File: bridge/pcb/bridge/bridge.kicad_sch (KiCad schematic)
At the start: 3 parts, among them J1 Motor_Control_Connector, J2 General_Use_Terminal, J3 Tachometer_Terminal

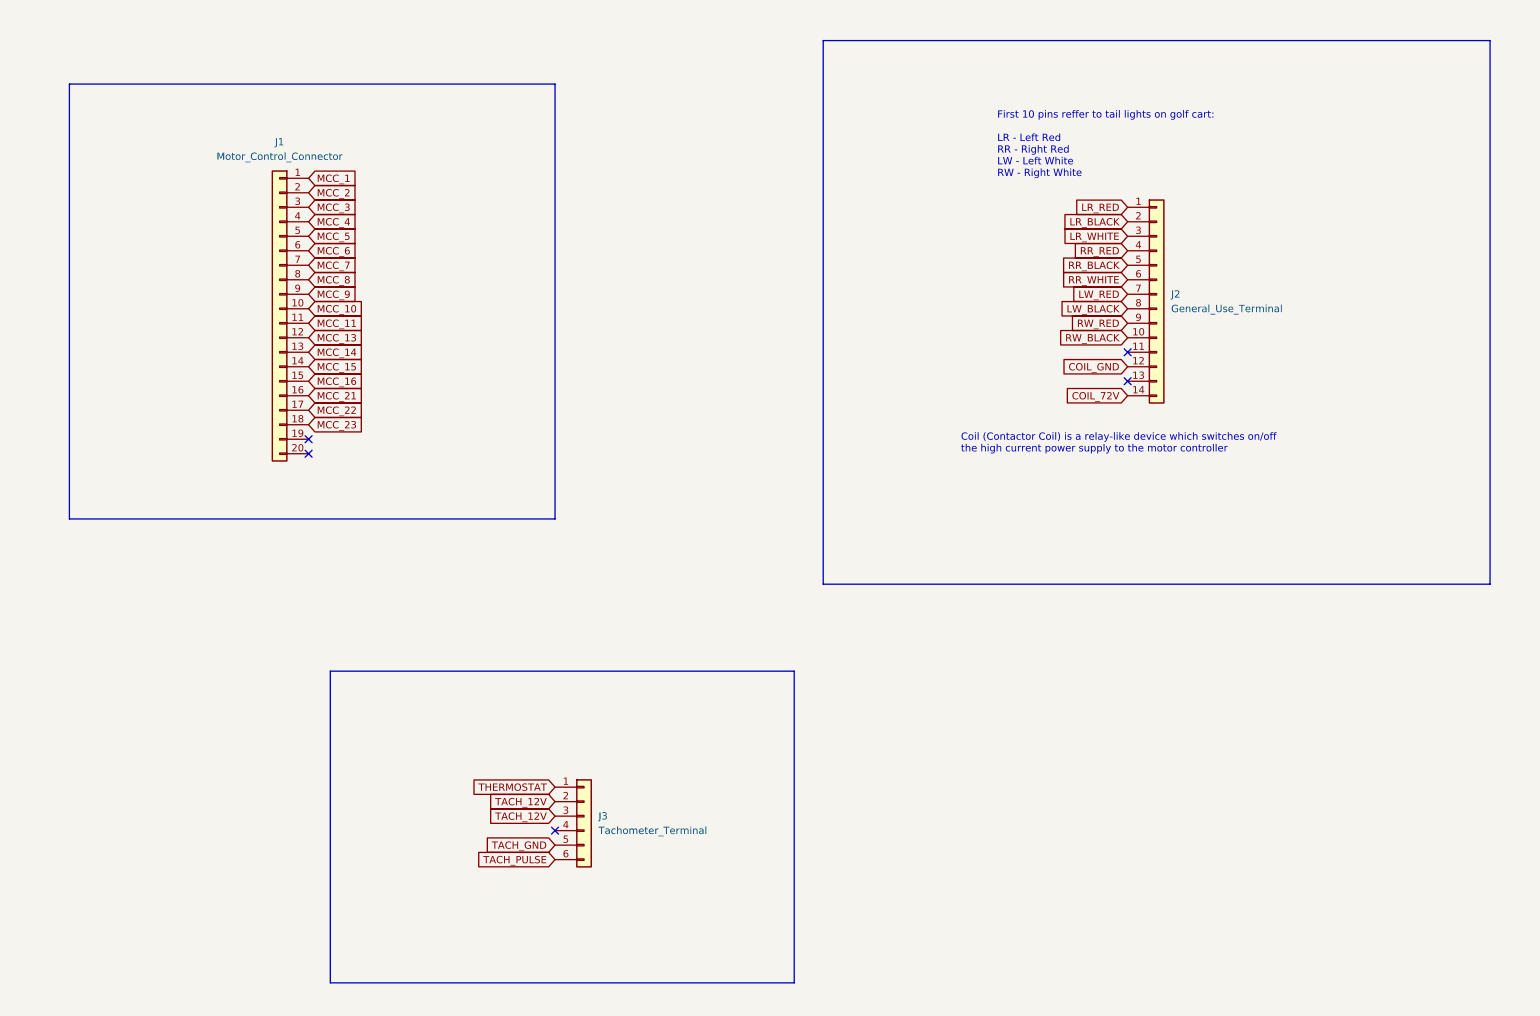
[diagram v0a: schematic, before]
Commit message: Completed schematic I/O connections
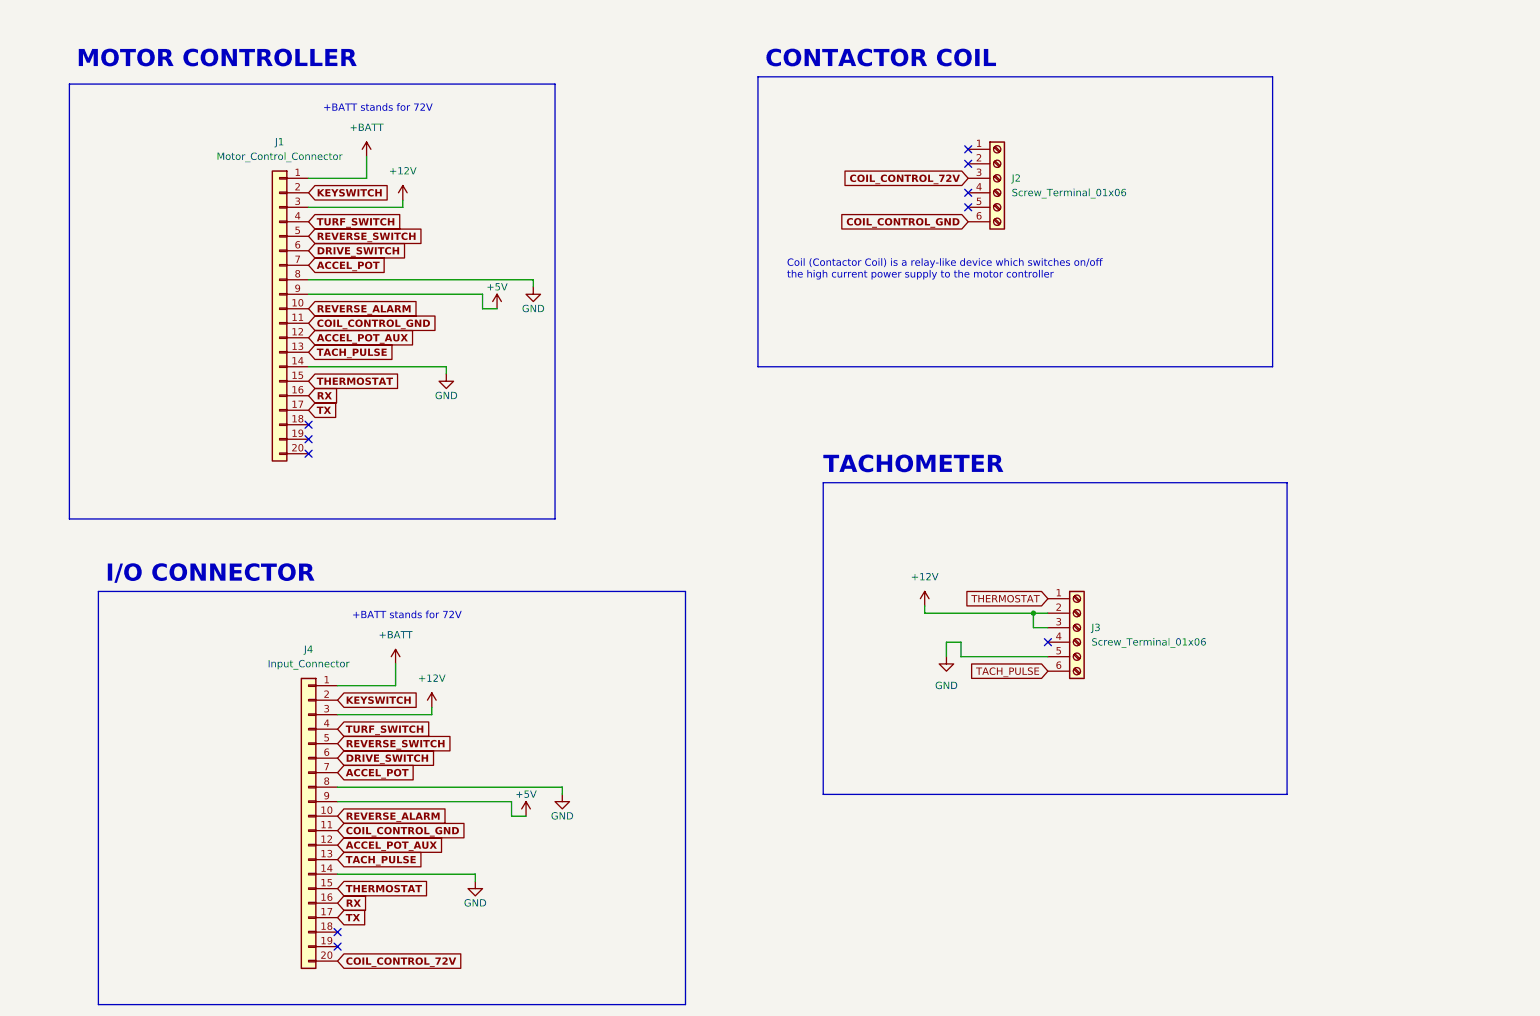
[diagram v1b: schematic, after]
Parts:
- removed J2: General_Use_Terminal, symbol Connector_Generic:Conn_01x14
- removed J3: Tachometer_Terminal, symbol Connector_Generic:Conn_01x06
- added J2, J3: Screw_Terminal_01x06, symbol Connector:Screw_Terminal_01x06
- added J4: Input_Connector, symbol Connector_Generic:Conn_01x20
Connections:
- net MCC_14 is gone; now on net TACH_PULSE: J1.13 (Pin_13)
- net MCC_16 is gone; now on net THERMOSTAT: J1.15 (Pin_15)
- net MCC_8 is gone; now on net GND: J1.8 (Pin_8)
- net TACH_PULSE: now also J3.6 (Pin_6), J4.13 (Pin_13)
- net THERMOSTAT: now also J3.1 (Pin_1), J4.15 (Pin_15)
- net MCC_1 renamed +BATT
- net +BATT: now also J4.1 (Pin_1)
- net MCC_10 renamed REVERSE_ALARM
- net REVERSE_ALARM: now also J4.10 (Pin_10)
- net MCC_11 renamed COIL_CONTROL_GND
- net COIL_CONTROL_GND: now also J2.6 (Pin_6), J4.11 (Pin_11)
- net MCC_13 renamed ACCEL_POT_AUX
- net ACCEL_POT_AUX: now also J4.12 (Pin_12)
- net MCC_15 renamed GND
- net GND: now also J3.5 (Pin_5), J4.14 (Pin_14), J4.8 (Pin_8)
- net MCC_2 renamed KEYSWITCH
- net KEYSWITCH: now also J4.2 (Pin_2)
- net MCC_21 renamed RX
- net RX: now also J4.16 (Pin_16)
- net MCC_22 renamed TX
- net TX: now also J4.17 (Pin_17)
- net MCC_23: no longer names the net of J1.18 (Pin_18)
- net MCC_3 renamed +12V
- net +12V: now also J3.2 (Pin_2), J3.3 (Pin_3), J4.3 (Pin_3)
- net MCC_4 renamed TURF_SWITCH
- net TURF_SWITCH: now also J4.4 (Pin_4)
- net MCC_5 renamed REVERSE_SWITCH
- net REVERSE_SWITCH: now also J4.5 (Pin_5)
- net MCC_6 renamed DRIVE_SWITCH
- net DRIVE_SWITCH: now also J4.6 (Pin_6)
- net MCC_7 renamed ACCEL_POT
- net ACCEL_POT: now also J4.7 (Pin_7)
- net MCC_9 renamed +5V
- net +5V: now also J4.9 (Pin_9)
- new net COIL_CONTROL_72V: J2.3 (Pin_3), J4.20 (Pin_20)
- no-connect marks 5 -> 10
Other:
- note added: "+BATT stands for 72V"
- note added: "CONTACTOR COIL"
- note added: "I/O CONNECTOR"
- note added: "MOTOR CONTROLLER"
- note added: "TACHOMETER"
- note removed: "First 10 pins reffer to tail lights on golf cart: LR - Left Red RR - Right Red LW - Left White RW - Right White"

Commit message: Changed circuit board setup to one board bridge
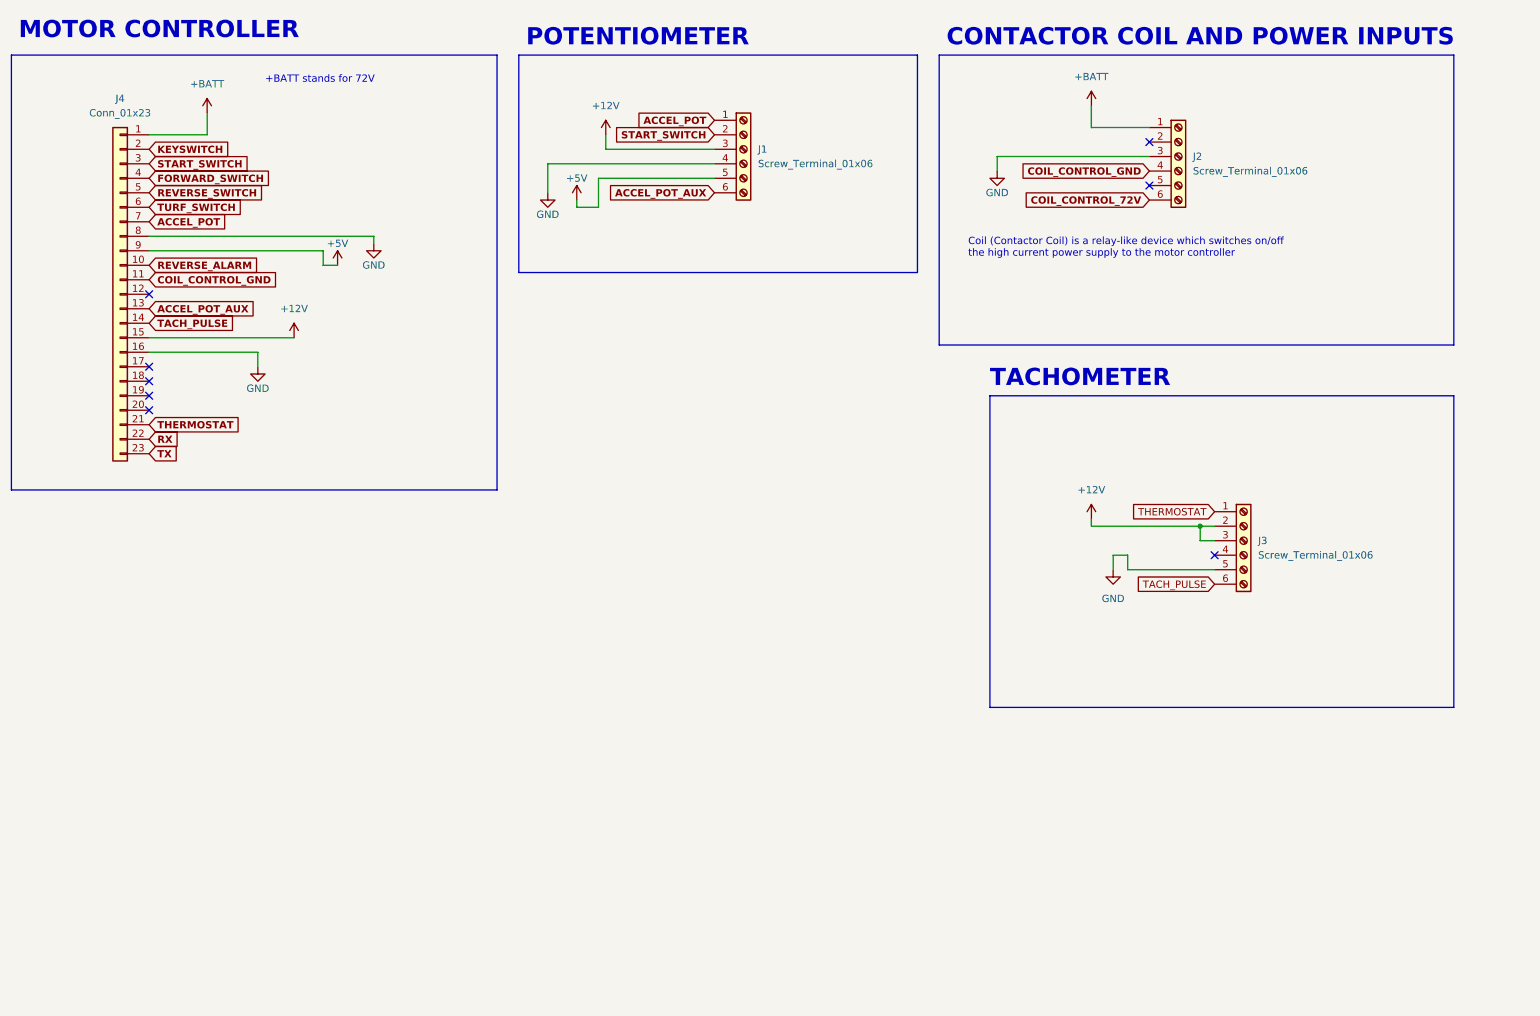
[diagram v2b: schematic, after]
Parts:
- removed J1: Motor_Control_Connector, symbol Connector_Generic:Conn_01x20
- removed J4: Input_Connector, symbol Connector_Generic:Conn_01x20
- added J1: Screw_Terminal_01x06, symbol Connector:Screw_Terminal_01x06
- added J4: Conn_01x23, Connector_TE-Connectivity:TE_AMPSEAL_1-776087-x_3Rows_23_P0.4mm_Horizontal, symbol Connector_Generic:Conn_01x23
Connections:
- net +12V: now also J1.3 (Pin_3), J4.15 (Pin_15)
- net +5V: now also J1.5 (Pin_5), J4.9 (Pin_9)
- net +BATT: now also J2.1 (Pin_1), J4.1 (Pin_1)
- net ACCEL_POT: now also J1.1 (Pin_1), J4.7 (Pin_7)
- net ACCEL_POT_AUX: now also J1.6 (Pin_6), J4.13 (Pin_13)
- net COIL_CONTROL_72V: now also J2.6 (Pin_6); no longer J2.3 (Pin_3)
- net COIL_CONTROL_GND: now also J2.4 (Pin_4), J4.11 (Pin_11); no longer J2.6 (Pin_6)
- net GND: now also J2.3 (Pin_3), J1.4 (Pin_4), J4.16 (Pin_16), J4.8 (Pin_8)
- net KEYSWITCH: now also J4.2 (Pin_2)
- net REVERSE_ALARM: now also J4.10 (Pin_10)
- net REVERSE_SWITCH: now also J4.5 (Pin_5)
- net RX: now also J4.22 (Pin_22)
- net TACH_PULSE: now also J4.14 (Pin_14)
- net THERMOSTAT: now also J4.21 (Pin_21)
- net TURF_SWITCH: now also J4.6 (Pin_6)
- net TX: now also J4.23 (Pin_23)
- new net FORWARD_SWITCH: J4.4 (Pin_4)
- new net START_SWITCH: J1.2 (Pin_2), J4.3 (Pin_3)
- no-connect marks 10 -> 8
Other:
- note added: "CONTACTOR COIL AND POWER INPUTS"
- note added: "POTENTIOMETER"
- note removed: "CONTACTOR COIL"
- note removed: "I/O CONNECTOR"
- moved on the sheet: J2, J3

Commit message: Added basic functions to PCB
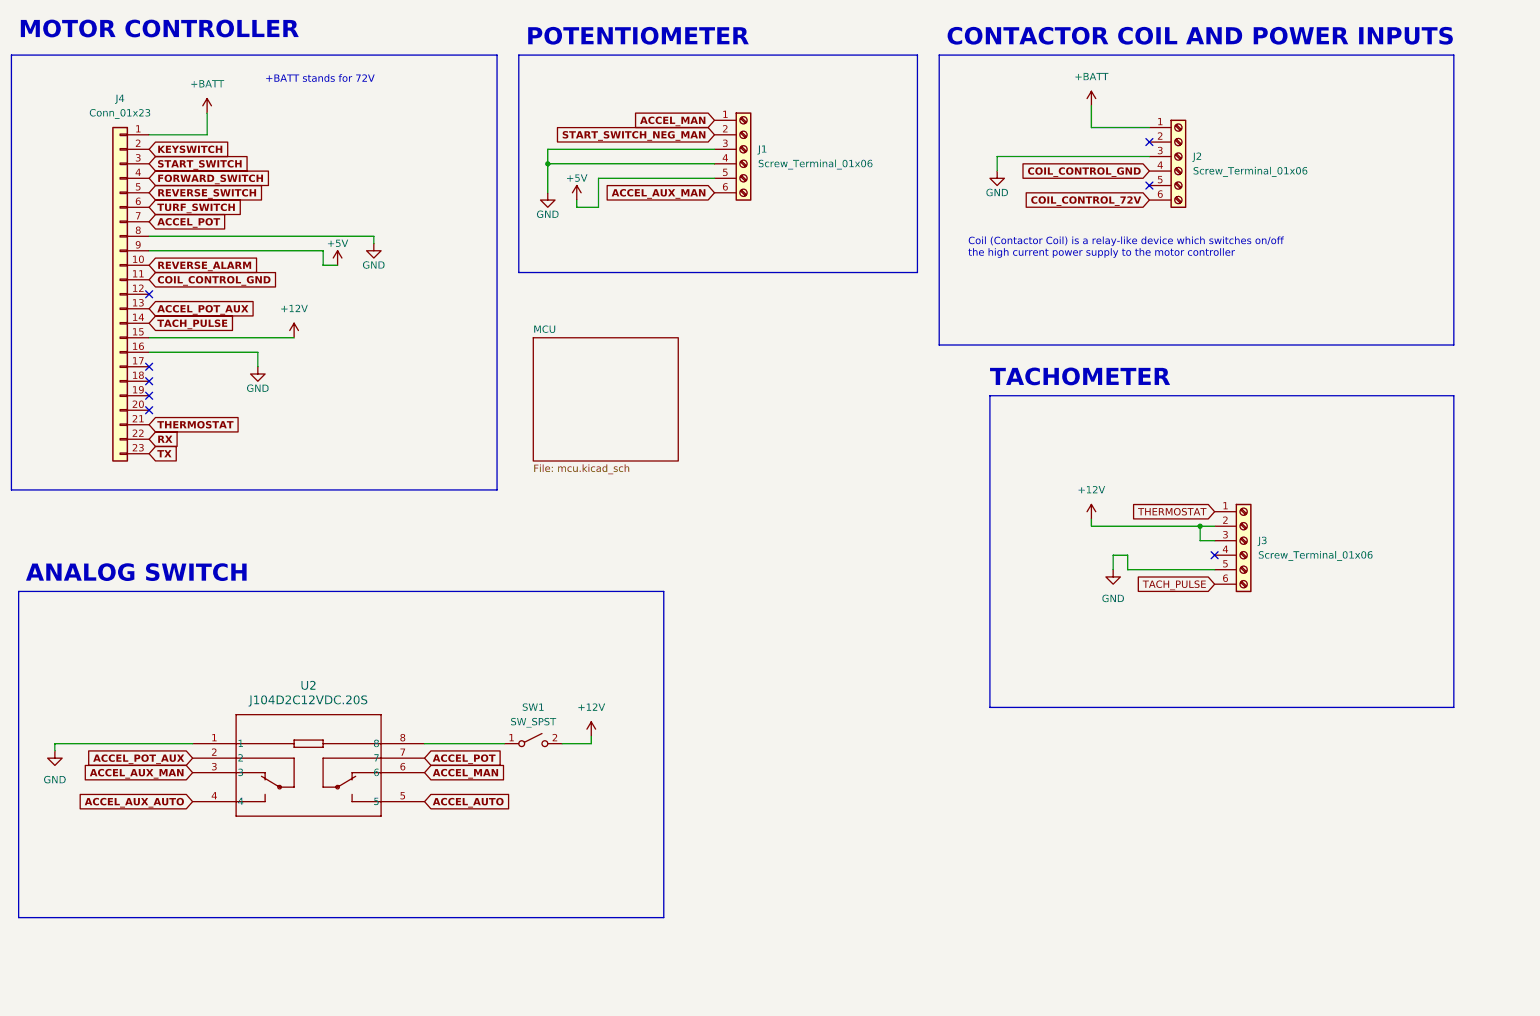
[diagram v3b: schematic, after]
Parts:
- added SW1: SW_SPST, Connector_PinHeader_2.54mm:PinHeader_1x02_P2.54mm_Vertical, symbol Switch:SW_SPST
- added U2: J104D2C12VDC.20S, bridge:RELAY8_J104D2C12VDC.20S_CRS, symbol bridge:J104D2C12VDC.20S
- J1, J2, J3: footprint (none) -> bridge:TE_2-1437667-9
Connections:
- net +12V: now also SW1.2 (B); no longer J1.3 (Pin_3)
- net ACCEL_POT: now also U2.7; no longer J1.1 (Pin_1)
- net ACCEL_POT_AUX: now also U2.2; no longer J1.6 (Pin_6)
- net GND: now also J1.3 (Pin_3), U2.1
- net START_SWITCH: no longer J1.2 (Pin_2)
- new net: SW1.1 (A), U2.8
- new net ACCEL_AUTO: U2.5
- new net ACCEL_AUX_AUTO: U2.4
- new net ACCEL_AUX_MAN: J1.6 (Pin_6), U2.3
- new net ACCEL_MAN: J1.1 (Pin_1), U2.6
- new net START_SWITCH_NEG_MAN: J1.2 (Pin_2)
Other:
- added sheet MCU (mcu.kicad_sch)
- note added: "ANALOG SWITCH"

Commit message: Fixed issues, added DAC
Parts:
- added D2, D3, D4, D5: GREEN, LED_THT:LED_D5.0mm, symbol Device:LED
- added R6, R7: 24k, Resistor_THT:R_Axial_DIN0309_L9.0mm_D3.2mm_P12.70mm_Horizontal, symbol Device:R
- added R8: 10k, Resistor_THT:R_Axial_DIN0309_L9.0mm_D3.2mm_P12.70mm_Horizontal, symbol Device:R
- added R9: 144k, Resistor_THT:R_Axial_DIN0309_L9.0mm_D3.2mm_P12.70mm_Horizontal, symbol Device:R
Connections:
- net +12V: now also R7.1
- net +5V: now also R8.1
- net +BATT: now also R9.1
- net GND: now also D2.1 (K), D3.1 (K), D4.1 (K), D5.1 (K)
- net at SW1.1 (A), U2.8: now also R6.1
- net ACCEL_AUX_AUTO: no longer names the net of U2.4
- new net 12V_LED_A: D3.2 (A), R7.2
- new net 5V_LED_A: D4.2 (A), R8.2
- new net 72V_LED_A: D5.2 (A), R9.2
- new net AUTO_MAN_LED_A: D2.2 (A), R6.2
- no-connect marks 8 -> 9
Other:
- note added: "STATUS LEDS"
- moved on the sheet: SW1
